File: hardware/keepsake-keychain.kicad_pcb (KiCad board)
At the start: 2 copper layers, 67 parts, among them Q1 MMFTP4042K, Q2 MMFTP4042K, Q3 MMFTP4042K, Q4 MMFTP4042K, SW1 SPDT Power Switch, SW2 PTS636 SK25J SMTR LFS, U1 74HC595 RED Shift Register, U2 74HC595 GREEN Shift Register, U3 74HC595 BLUE Shift Register, U4 Op Amp, U5 ATTINY1614, U6 MEMS Microphone

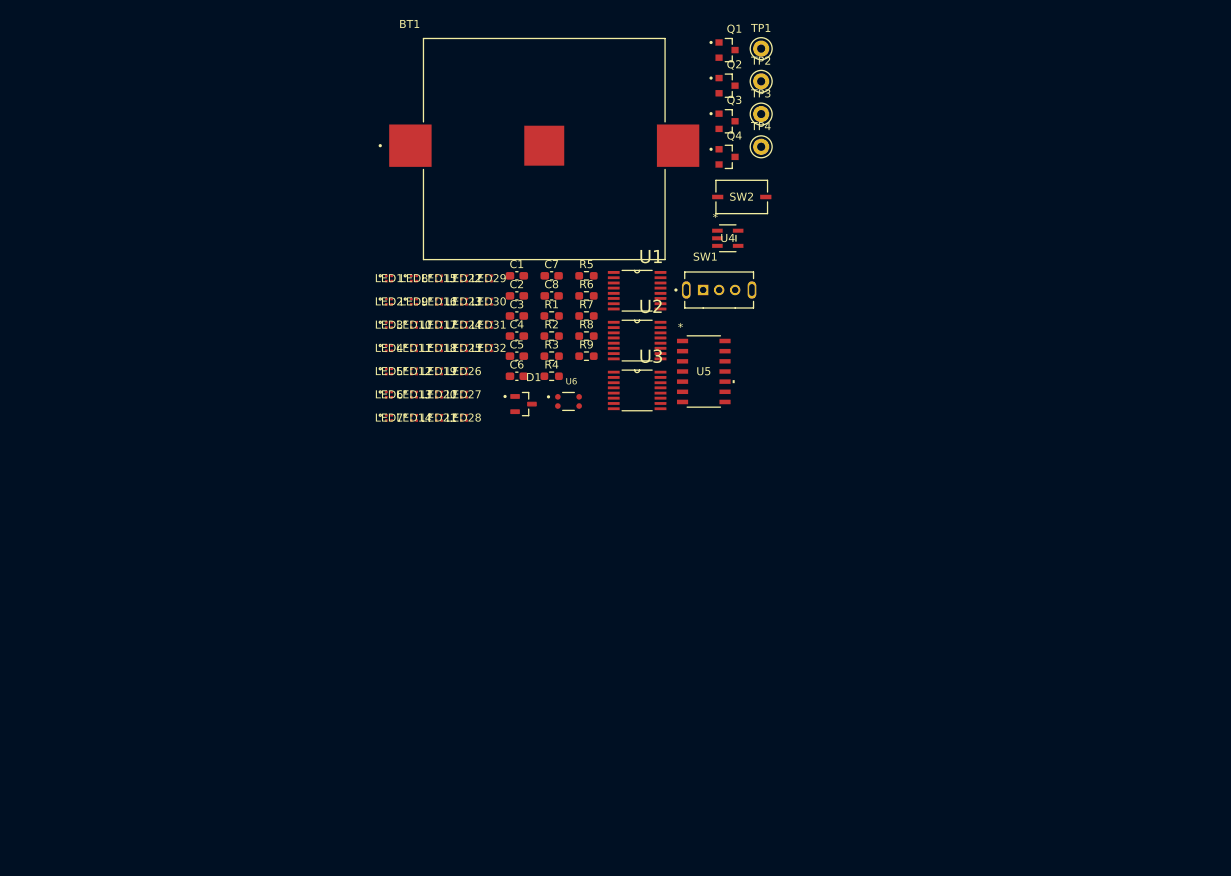
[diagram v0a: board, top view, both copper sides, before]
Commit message: Swap push button and slide switch for better options
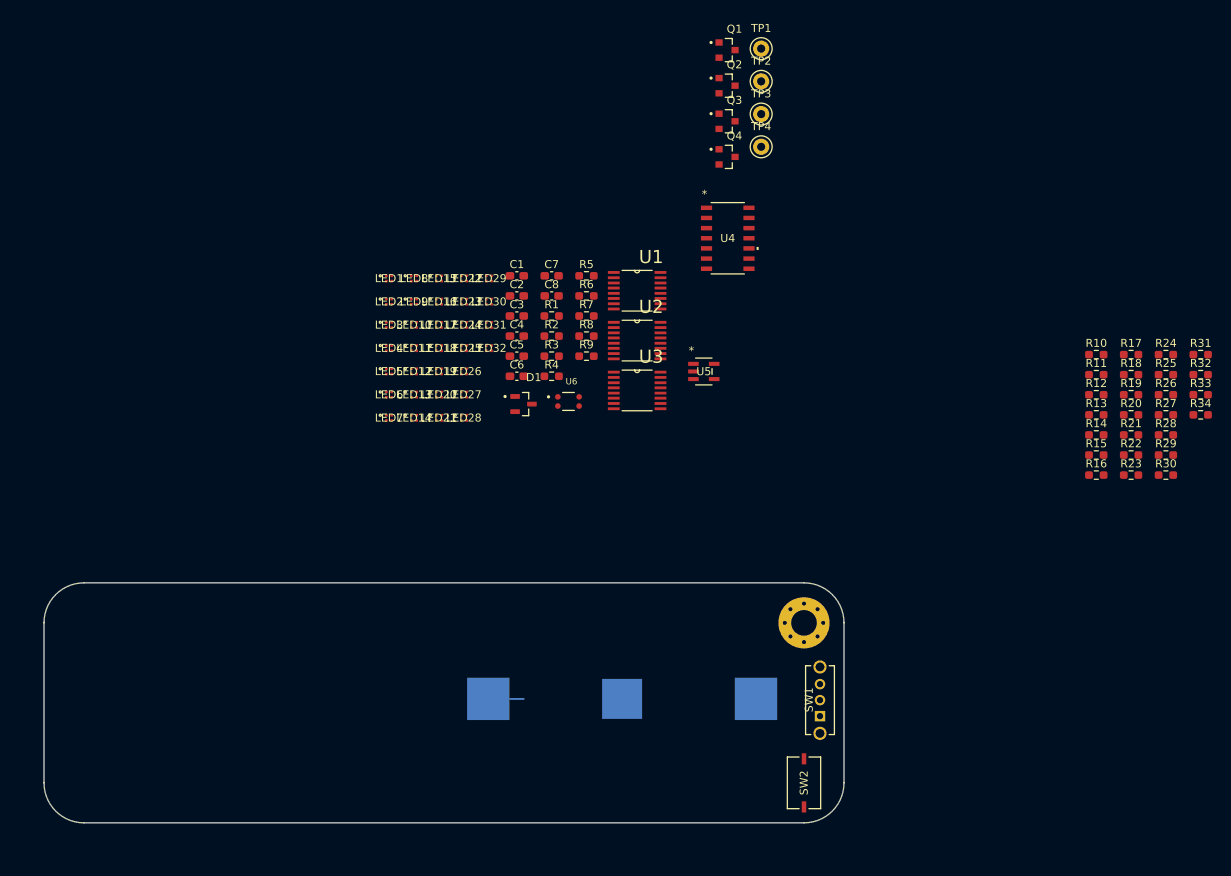
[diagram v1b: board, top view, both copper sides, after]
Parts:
- added H1: MountingHole, MountingHole:MountingHole_3.2mm_M3_Pad_Via, F.Cu at (178.5, 108.0)
- added R10: 100, Resistor_SMD:R_0603_1608Metric_Pad0.98x0.95mm_HandSolder, F.Cu at (215.0, 74.5)
- added R11: 120, Resistor_SMD:R_0603_1608Metric_Pad0.98x0.95mm_HandSolder, F.Cu at (215.0, 77.0)
- added R12: 180, Resistor_SMD:R_0603_1608Metric_Pad0.98x0.95mm_HandSolder, F.Cu at (215.0, 79.5)
- added R13: 100, Resistor_SMD:R_0603_1608Metric_Pad0.98x0.95mm_HandSolder, F.Cu at (215.0, 82.0)
- added R14: 120, Resistor_SMD:R_0603_1608Metric_Pad0.98x0.95mm_HandSolder, F.Cu at (215.0, 84.5)
- added R15: 180, Resistor_SMD:R_0603_1608Metric_Pad0.98x0.95mm_HandSolder, F.Cu at (215.0, 87.0)
- added R16: 100, Resistor_SMD:R_0603_1608Metric_Pad0.98x0.95mm_HandSolder, F.Cu at (215.0, 89.5)
- added R17: 120, Resistor_SMD:R_0603_1608Metric_Pad0.98x0.95mm_HandSolder, F.Cu at (219.4, 74.5)
- added R18: 180, Resistor_SMD:R_0603_1608Metric_Pad0.98x0.95mm_HandSolder, F.Cu at (219.4, 77.0)
- added R19: 100, Resistor_SMD:R_0603_1608Metric_Pad0.98x0.95mm_HandSolder, F.Cu at (219.4, 79.5)
- added R20: 120, Resistor_SMD:R_0603_1608Metric_Pad0.98x0.95mm_HandSolder, F.Cu at (219.4, 82.0)
- added R21: 180, Resistor_SMD:R_0603_1608Metric_Pad0.98x0.95mm_HandSolder, F.Cu at (219.4, 84.5)
- added R22: 100, Resistor_SMD:R_0603_1608Metric_Pad0.98x0.95mm_HandSolder, F.Cu at (219.4, 87.0)
- added R23: 120, Resistor_SMD:R_0603_1608Metric_Pad0.98x0.95mm_HandSolder, F.Cu at (219.4, 89.5)
- added R24: 180, Resistor_SMD:R_0603_1608Metric_Pad0.98x0.95mm_HandSolder, F.Cu at (223.7, 74.5)
- added R25: 390K, Resistor_SMD:R_0603_1608Metric_Pad0.98x0.95mm_HandSolder, F.Cu at (223.7, 77.0)
- added R26: 10K, Resistor_SMD:R_0603_1608Metric_Pad0.98x0.95mm_HandSolder, F.Cu at (223.7, 79.5)
- added R27: 100K, Resistor_SMD:R_0603_1608Metric_Pad0.98x0.95mm_HandSolder, F.Cu at (223.7, 82.0)
- added R28: 10K, Resistor_SMD:R_0603_1608Metric_Pad0.98x0.95mm_HandSolder, F.Cu at (223.7, 84.5)
- added R29: 100K, Resistor_SMD:R_0603_1608Metric_Pad0.98x0.95mm_HandSolder, F.Cu at (223.7, 87.0)
- added R30: 100K, Resistor_SMD:R_0603_1608Metric_Pad0.98x0.95mm_HandSolder, F.Cu at (223.7, 89.5)
- added R31: 100K, Resistor_SMD:R_0603_1608Metric_Pad0.98x0.95mm_HandSolder, F.Cu at (228.1, 74.5)
- added R32: 100K, Resistor_SMD:R_0603_1608Metric_Pad0.98x0.95mm_HandSolder, F.Cu at (228.1, 77.0)
- added R33: 100K, Resistor_SMD:R_0603_1608Metric_Pad0.98x0.95mm_HandSolder, F.Cu at (228.1, 79.5)
- added R34: 100K, Resistor_SMD:R_0603_1608Metric_Pad0.98x0.95mm_HandSolder, F.Cu at (228.1, 82.0)
- BT1: moved to B.Cu
- R1: value 390K -> 100
- R2, R5, R8: value 100K -> 120
- R3: value 10K -> 180
- R4, R7: value 100K -> 100
- R6, R9: value 100K -> 180
- SW2: footprint 0_Push_Button:SW_PTS636_SK25J_SMTR_LFS_CNK -> 0_Tactile_Push_Button:SW_PTS636_SK25J_SMTR_LFS_CNK
- U1: value 74HC595 RED Shift Register -> 74HC595 BLUE Shift Register
- U3: value 74HC595 BLUE Shift Register -> 74HC595 RED Shift Register
- U4: value Op Amp -> ATTINY1614; footprint 0_Op_Amp:SOT-23-5_MC_MCH -> 0_ATtiny1614:SOIC14_SL_MCH
- U5: value ATTINY1614 -> Op Amp; footprint 0_ATtiny1614:SOIC14_SL_MCH -> 0_Op_Amp:SOT-23-5_MC_MCH
- moved SW2 73.6 mm to (178.5, 128.0), turned to 90 degrees
- moved BT1 69.8 mm to (155.8, 117.5), turned to 180 degrees
- moved SW1 52.8 mm to (180.5, 117.7), turned to 90 degrees
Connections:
- C7 pad 2: Net-(U4-VIN+) -> Net-(U5-VIN+)
- D1 pad 1: Net-(U4-VOUT) -> Net-(U5-VOUT)
- LED1 pad 1: unconnected-(LED1-Pad1) -> BLUE_0
- LED1 pad 2: unconnected-(LED1-Pad2) -> GREEN_0
- LED1 pad 3: unconnected-(LED1-Pad3) -> RED_0
- LED10 pad 1: unconnected-(LED10-Pad1) -> BLUE_2
- LED10 pad 2: unconnected-(LED10-Pad2) -> GREEN_2
- LED10 pad 3: unconnected-(LED10-Pad3) -> RED_2
- LED11 pad 1: unconnected-(LED11-Pad1) -> BLUE_4
- LED11 pad 2: unconnected-(LED11-Pad2) -> GREEN_4
- LED11 pad 3: unconnected-(LED11-Pad3) -> RED_4
- LED12 pad 1: unconnected-(LED12-Pad1) -> BLUE_6
- LED12 pad 2: unconnected-(LED12-Pad2) -> GREEN_6
- LED12 pad 3: unconnected-(LED12-Pad3) -> RED_6
- LED13 pad 1: unconnected-(LED13-Pad1) -> BLUE_1
- LED13 pad 2: unconnected-(LED13-Pad2) -> GREEN_1
- LED13 pad 3: unconnected-(LED13-Pad3) -> RED_1
- LED14 pad 1: unconnected-(LED14-Pad1) -> BLUE_3
- LED14 pad 2: unconnected-(LED14-Pad2) -> GREEN_3
- LED14 pad 3: unconnected-(LED14-Pad3) -> RED_3
- LED15 pad 1: unconnected-(LED15-Pad1) -> BLUE_5
- LED15 pad 2: unconnected-(LED15-Pad2) -> GREEN_5
- LED15 pad 3: unconnected-(LED15-Pad3) -> RED_5
- LED16 pad 1: unconnected-(LED16-Pad1) -> BLUE_7
- LED16 pad 2: unconnected-(LED16-Pad2) -> GREEN_7
- LED16 pad 3: unconnected-(LED16-Pad3) -> RED_7
- LED17 pad 1: unconnected-(LED17-Pad1) -> BLUE_0
- LED17 pad 2: unconnected-(LED17-Pad2) -> GREEN_0
- LED17 pad 3: unconnected-(LED17-Pad3) -> RED_0
- LED18 pad 1: unconnected-(LED18-Pad1) -> BLUE_2
- LED18 pad 2: unconnected-(LED18-Pad2) -> GREEN_2
- LED18 pad 3: unconnected-(LED18-Pad3) -> RED_2
- LED19 pad 1: unconnected-(LED19-Pad1) -> BLUE_4
- LED19 pad 2: unconnected-(LED19-Pad2) -> GREEN_4
- LED19 pad 3: unconnected-(LED19-Pad3) -> RED_4
- LED2 pad 1: unconnected-(LED2-Pad1) -> BLUE_2
- LED2 pad 2: unconnected-(LED2-Pad2) -> GREEN_2
- LED2 pad 3: unconnected-(LED2-Pad3) -> RED_2
- LED20 pad 1: unconnected-(LED20-Pad1) -> BLUE_6
- LED20 pad 2: unconnected-(LED20-Pad2) -> GREEN_6
- LED20 pad 3: unconnected-(LED20-Pad3) -> RED_6
- LED21 pad 1: unconnected-(LED21-Pad1) -> BLUE_1
- LED21 pad 2: unconnected-(LED21-Pad2) -> GREEN_1
- LED21 pad 3: unconnected-(LED21-Pad3) -> RED_1
- LED22 pad 1: unconnected-(LED22-Pad1) -> BLUE_3
- LED22 pad 2: unconnected-(LED22-Pad2) -> GREEN_3
- LED22 pad 3: unconnected-(LED22-Pad3) -> RED_3
- LED23 pad 1: unconnected-(LED23-Pad1) -> BLUE_5
- LED23 pad 2: unconnected-(LED23-Pad2) -> GREEN_5
- LED23 pad 3: unconnected-(LED23-Pad3) -> RED_5
- LED24 pad 1: unconnected-(LED24-Pad1) -> BLUE_7
- LED24 pad 2: unconnected-(LED24-Pad2) -> GREEN_7
- LED24 pad 3: unconnected-(LED24-Pad3) -> RED_7
- LED25 pad 1: unconnected-(LED25-Pad1) -> BLUE_0
- LED25 pad 2: unconnected-(LED25-Pad2) -> GREEN_0
- LED25 pad 3: unconnected-(LED25-Pad3) -> RED_0
- LED26 pad 1: unconnected-(LED26-Pad1) -> BLUE_2
- LED26 pad 2: unconnected-(LED26-Pad2) -> GREEN_2
- LED26 pad 3: unconnected-(LED26-Pad3) -> RED_2
- LED27 pad 1: unconnected-(LED27-Pad1) -> BLUE_4
- LED27 pad 2: unconnected-(LED27-Pad2) -> GREEN_4
- LED27 pad 3: unconnected-(LED27-Pad3) -> RED_4
- LED28 pad 1: unconnected-(LED28-Pad1) -> BLUE_6
- LED28 pad 2: unconnected-(LED28-Pad2) -> GREEN_6
- LED28 pad 3: unconnected-(LED28-Pad3) -> RED_6
- LED29 pad 1: unconnected-(LED29-Pad1) -> BLUE_1
- LED29 pad 2: unconnected-(LED29-Pad2) -> GREEN_1
- LED29 pad 3: unconnected-(LED29-Pad3) -> RED_1
- LED3 pad 1: unconnected-(LED3-Pad1) -> BLUE_4
- LED3 pad 2: unconnected-(LED3-Pad2) -> GREEN_4
- LED3 pad 3: unconnected-(LED3-Pad3) -> RED_4
- LED30 pad 1: unconnected-(LED30-Pad1) -> BLUE_3
- LED30 pad 2: unconnected-(LED30-Pad2) -> GREEN_3
- LED30 pad 3: unconnected-(LED30-Pad3) -> RED_3
- LED31 pad 1: unconnected-(LED31-Pad1) -> BLUE_5
- LED31 pad 2: unconnected-(LED31-Pad2) -> GREEN_5
- LED31 pad 3: unconnected-(LED31-Pad3) -> RED_5
- LED32 pad 1: unconnected-(LED32-Pad1) -> BLUE_7
- LED32 pad 2: unconnected-(LED32-Pad2) -> GREEN_7
- LED32 pad 3: unconnected-(LED32-Pad3) -> RED_7
- LED4 pad 1: unconnected-(LED4-Pad1) -> BLUE_6
- LED4 pad 2: unconnected-(LED4-Pad2) -> GREEN_6
- LED4 pad 3: unconnected-(LED4-Pad3) -> RED_6
- LED5 pad 1: unconnected-(LED5-Pad1) -> BLUE_1
- LED5 pad 2: unconnected-(LED5-Pad2) -> GREEN_1
- LED5 pad 3: unconnected-(LED5-Pad3) -> RED_1
- LED6 pad 1: unconnected-(LED6-Pad1) -> BLUE_3
- LED6 pad 2: unconnected-(LED6-Pad2) -> GREEN_3
- LED6 pad 3: unconnected-(LED6-Pad3) -> RED_3
- LED7 pad 1: unconnected-(LED7-Pad1) -> BLUE_5
- LED7 pad 2: unconnected-(LED7-Pad2) -> GREEN_5
- LED7 pad 3: unconnected-(LED7-Pad3) -> RED_5
- LED8 pad 1: unconnected-(LED8-Pad1) -> BLUE_7
- LED8 pad 2: unconnected-(LED8-Pad2) -> GREEN_7
- LED8 pad 3: unconnected-(LED8-Pad3) -> RED_7
- LED9 pad 1: unconnected-(LED9-Pad1) -> BLUE_0
- LED9 pad 2: unconnected-(LED9-Pad2) -> GREEN_0
- LED9 pad 3: unconnected-(LED9-Pad3) -> RED_0
- Q1 pad 1: Net-(Q1-Pad1) -> S_ROW_0
- Q2 pad 1: Net-(Q2-Pad1) -> S_ROW_1
- Q3 pad 1: Net-(Q3-Pad1) -> S_ROW_2
- Q4 pad 1: Net-(Q4-Pad1) -> S_ROW_3
- R1 pad 1: Net-(U4-VOUT) -> BLUE_0
- R1 pad 2: Net-(U4-VIN-) -> Net-(U1-Q0)
- R2 pad 1: +3V3 -> GREEN_0
- R2 pad 2: /BIAS -> Net-(U2-Q0)
- R3 pad 1: Net-(U4-VIN-) -> RED_0
- R3 pad 2: /BIAS -> Net-(U3-Q0)
- R4 pad 1: /BIAS -> BLUE_1
- R4 pad 2: GND -> Net-(U1-Q1)
- R5 pad 1: MIC -> GREEN_1
- R5 pad 2: GND -> Net-(U2-Q1)
- R6 pad 1: S_ROW_0 -> RED_1
- R6 pad 2: Net-(Q1-Pad1) -> Net-(U3-Q1)
- R7 pad 1: S_ROW_1 -> BLUE_2
- R7 pad 2: Net-(Q2-Pad1) -> Net-(U1-Q2)
- R8 pad 1: S_ROW_2 -> GREEN_2
- R8 pad 2: Net-(Q3-Pad1) -> Net-(U2-Q2)
- R9 pad 1: S_ROW_3 -> RED_2
- R9 pad 2: Net-(Q4-Pad1) -> Net-(U3-Q2)
- SW2 pad 1: Net-(U5-PB0) -> Net-(U4-PB0)
- TP1 pad 1: MIC -> Net-(U4-PA0/*RESET/UPDI)
- TP2 pad 1: Net-(U5-PA0/*RESET/UPDI) -> MIC
- TP3 pad 1: Net-(U5-TOSC1/PB3) -> Net-(U4-TOSC1/PB3)
- TP4 pad 1: Net-(U5-TOSC2/PB2) -> Net-(U4-TOSC2/PB2)
- U1 pad 1: unconnected-(U1-Q1-Pad1) -> Net-(U1-Q1)
- U1 pad 14: DATA -> Net-(U1-DS)
- U1 pad 15: unconnected-(U1-Q0-Pad15) -> Net-(U1-Q0)
- U1 pad 2: unconnected-(U1-Q2-Pad2) -> Net-(U1-Q2)
- U1 pad 3: unconnected-(U1-Q3-Pad3) -> Net-(U1-Q3)
- U1 pad 4: unconnected-(U1-Q4-Pad4) -> Net-(U1-Q4)
- U1 pad 5: unconnected-(U1-Q5-Pad5) -> Net-(U1-Q5)
- U1 pad 6: unconnected-(U1-Q6-Pad6) -> Net-(U1-Q6)
- U1 pad 7: unconnected-(U1-Q7-Pad7) -> Net-(U1-Q7)
- U2 pad 1: unconnected-(U2-Q1-Pad1) -> Net-(U2-Q1)
- U2 pad 15: unconnected-(U2-Q0-Pad15) -> Net-(U2-Q0)
- U2 pad 2: unconnected-(U2-Q2-Pad2) -> Net-(U2-Q2)
- U2 pad 3: unconnected-(U2-Q3-Pad3) -> Net-(U2-Q3)
- U2 pad 4: unconnected-(U2-Q4-Pad4) -> Net-(U2-Q4)
- U2 pad 5: unconnected-(U2-Q5-Pad5) -> Net-(U2-Q5)
- U2 pad 6: unconnected-(U2-Q6-Pad6) -> Net-(U2-Q6)
- U2 pad 7: unconnected-(U2-Q7-Pad7) -> Net-(U2-Q7)
- U3 pad 1: unconnected-(U3-Q1-Pad1) -> Net-(U3-Q1)
- U3 pad 15: unconnected-(U3-Q0-Pad15) -> Net-(U3-Q0)
- U3 pad 2: unconnected-(U3-Q2-Pad2) -> Net-(U3-Q2)
- U3 pad 3: unconnected-(U3-Q3-Pad3) -> Net-(U3-Q3)
- U3 pad 4: unconnected-(U3-Q4-Pad4) -> Net-(U3-Q4)
- U3 pad 5: unconnected-(U3-Q5-Pad5) -> Net-(U3-Q5)
- U3 pad 6: unconnected-(U3-Q6-Pad6) -> Net-(U3-Q6)
- U3 pad 7: unconnected-(U3-Q7-Pad7) -> Net-(U3-Q7)
- U4 pad 1: Net-(U4-VOUT) -> +3V3
- U4 pad 2: GND -> S_ROW_0
- U4 pad 3: Net-(U4-VIN+) -> S_ROW_1
- U4 pad 4: Net-(U4-VIN-) -> S_ROW_2
- U4 pad 5: +3V3 -> S_ROW_3
- U5 pad 1: +3V3 -> Net-(U5-VOUT)
- U5 pad 2: S_ROW_0 -> GND
- U5 pad 3: S_ROW_1 -> Net-(U5-VIN+)
- U5 pad 4: S_ROW_2 -> Net-(U5-VIN-)
- U5 pad 5: S_ROW_3 -> +3V3
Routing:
- net Net-(BT1-Pad1): track 0.00 -> 1.73 mm
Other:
- board outline added: 100 x 30 mm

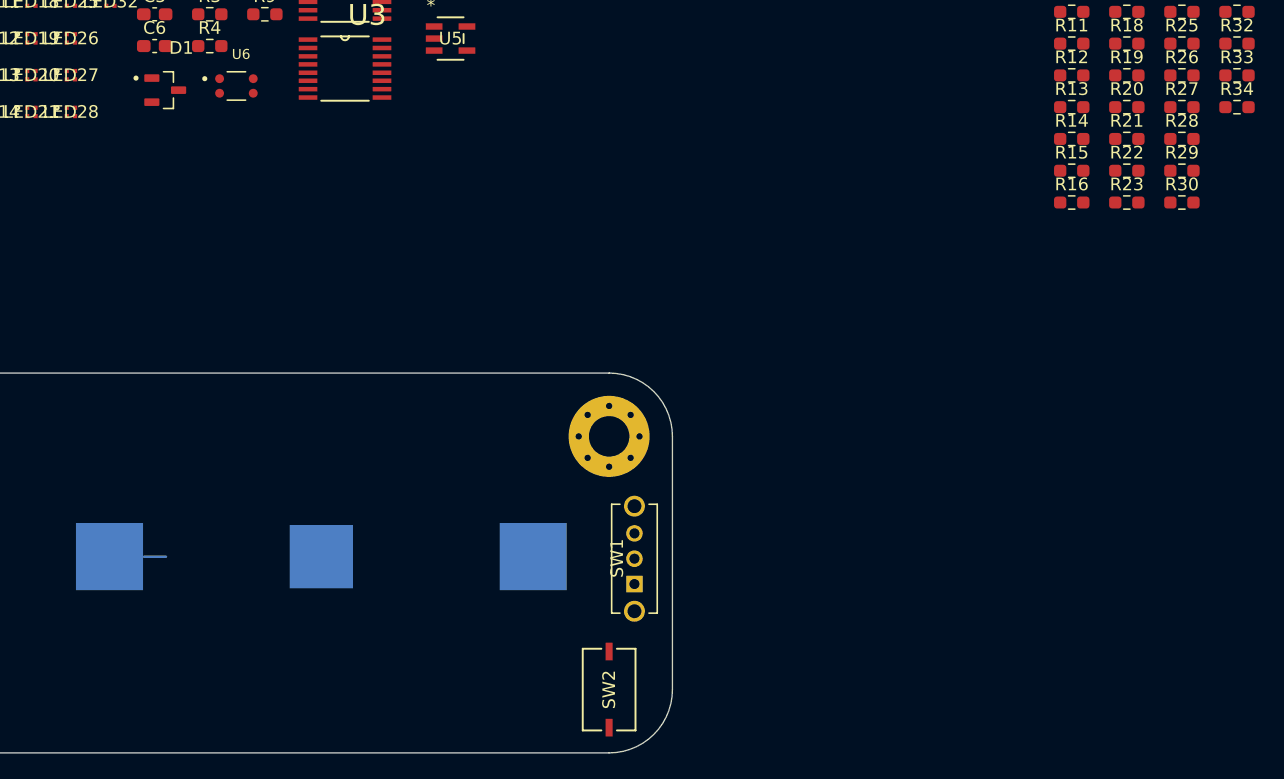
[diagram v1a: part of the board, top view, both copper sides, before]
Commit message: Attach models. Complete schematic, pass ERC.
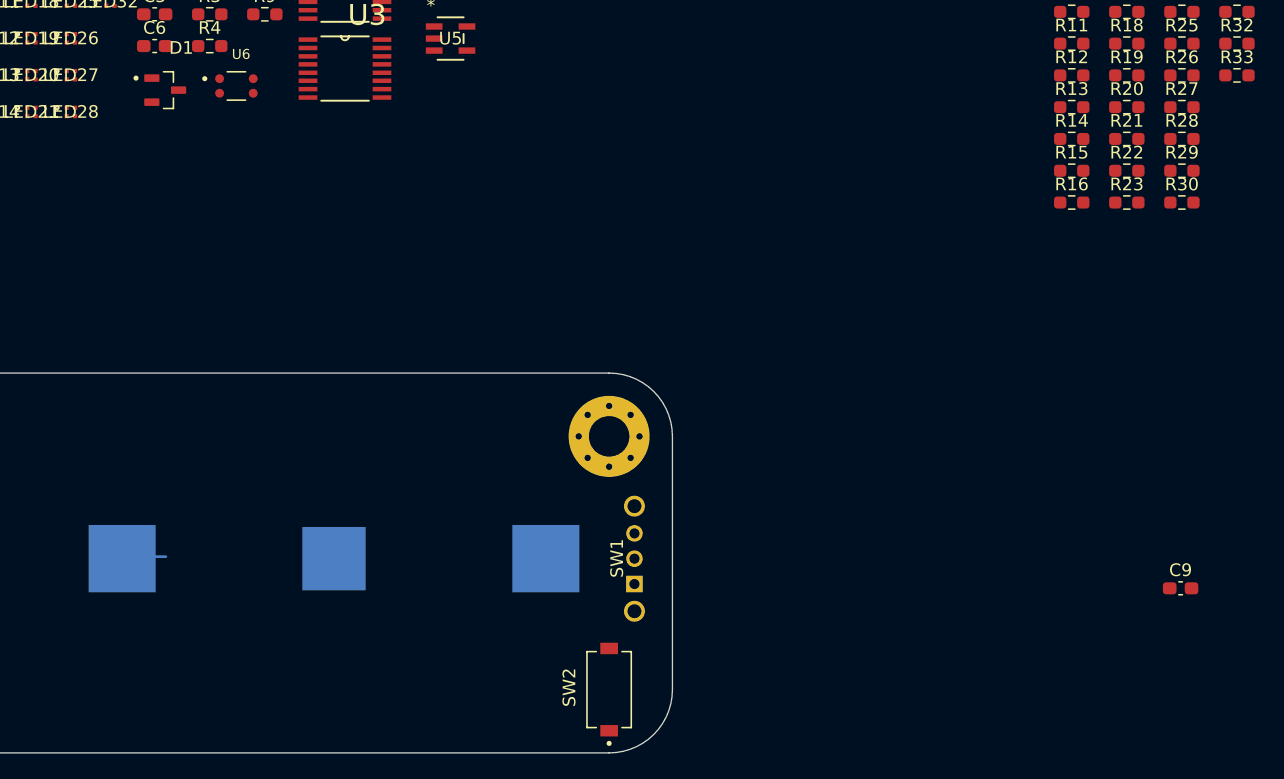
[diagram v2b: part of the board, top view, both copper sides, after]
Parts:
- removed R34: 100K, Resistor_SMD:R_0603_1608Metric_Pad0.98x0.95mm_HandSolder
- added C9: 1uF, Capacitor_SMD:C_0603_1608Metric_Pad1.08x0.95mm_HandSolder, F.Cu at (223.6, 120.0)
- R25: value 390K -> 220K
- SW2: footprint 0_Tactile_Push_Button:SW_PTS636_SK25J_SMTR_LFS_CNK -> 0_Tactile_Push_Button:SW_PTS636_SM43J_SMTR_LFS
- moved BT1 1.01 mm to (156.8, 117.7)
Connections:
- BT1 pad 1_1: Net-(BT1-Pad1) -> (no net)
- C1 pad 1: GND -> +3V3
- C1 pad 2: +3V3 -> GND
- C2 pad 1: GND -> +3V3
- C2 pad 2: +3V3 -> GND
- C3 pad 1: GND -> +3V3
- C3 pad 2: +3V3 -> GND
- C6 pad 1: GND -> +3V3
- C6 pad 2: MIC -> GND
- C7 pad 1: Net-(U6-OUTPUT) -> GND
- C7 pad 2: Net-(U5-VIN+) -> MIC
- C8 pad 1: /BIAS -> Net-(U6-OUTPUT)
- C8 pad 2: GND -> Net-(U5-VIN+)
- R29 pad 1: MIC -> /BIAS
- R30 pad 1: /BIAS -> S_ROW_0
- R30 pad 2: GND -> +3V3
- R31 pad 1: S_ROW_0 -> S_ROW_1
- R32 pad 1: S_ROW_1 -> S_ROW_2
- R33 pad 1: S_ROW_2 -> S_ROW_3

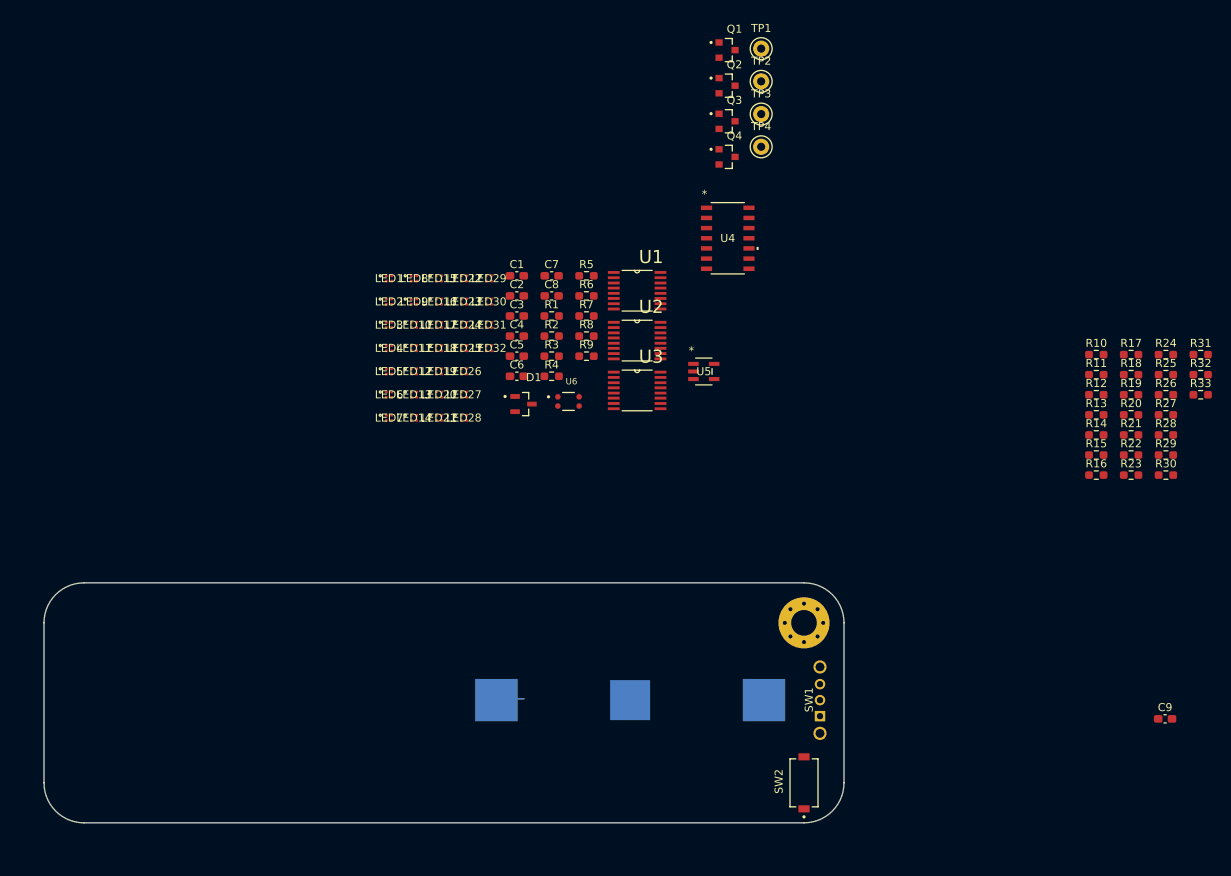
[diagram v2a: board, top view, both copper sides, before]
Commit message: Place LED passives in line
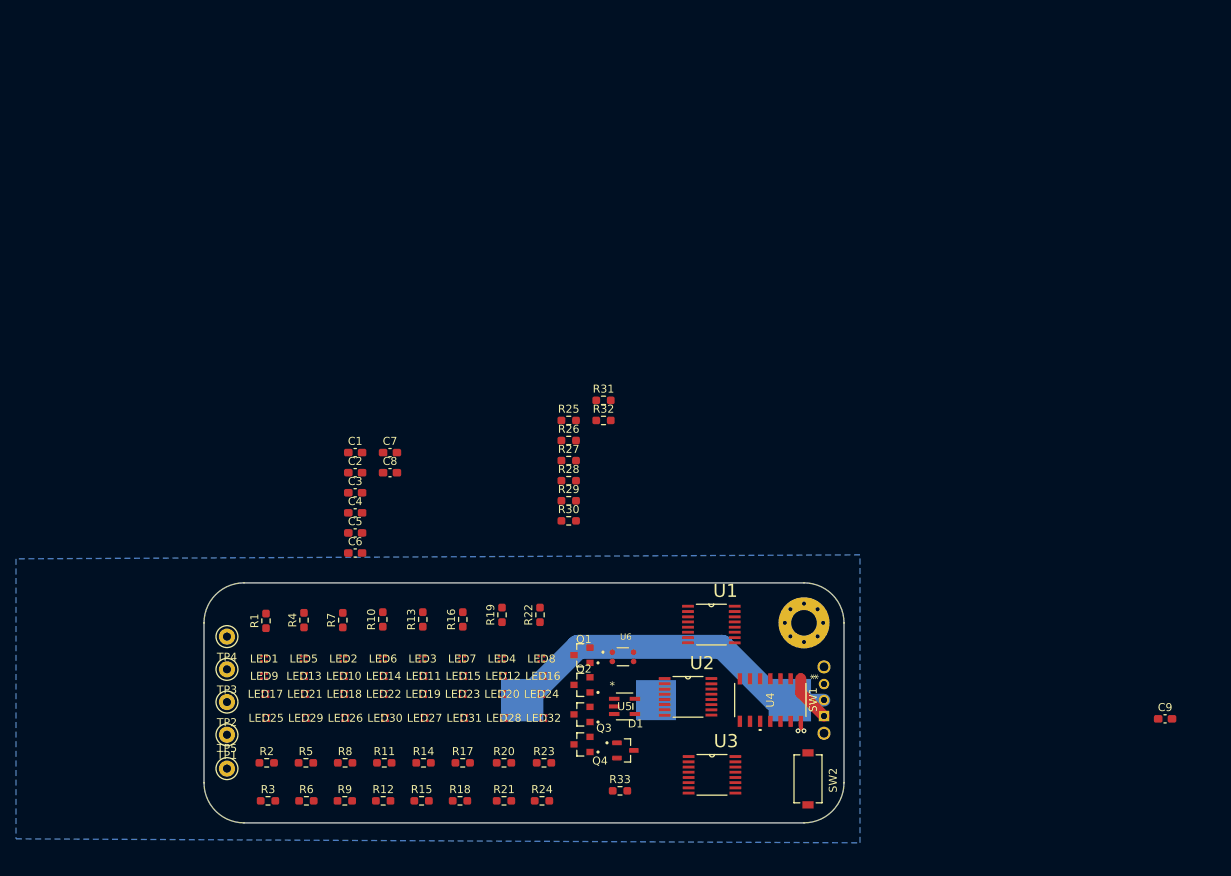
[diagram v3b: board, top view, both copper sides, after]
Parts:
- added TP5: 5002, digikey-footprints:Test_Point_D1.02mm, F.Cu at (106.4, 126.2)
- moved TP1 108.7 mm to (106.4, 122.0), turned to 180 degrees
- moved R12 102.6 mm to (125.9, 130.2)
- moved TP2 102.4 mm to (106.4, 117.9), turned to 180 degrees
- moved R11 101.4 mm to (126.0, 125.5)
- moved R18 99.4 mm to (135.5, 130.2)
- moved R17 97.9 mm to (135.8, 125.5)
- moved TP3 96.3 mm to (106.4, 113.8), turned to 180 degrees
- moved R24 95.9 mm to (145.8, 130.2)
- moved R10 95.1 mm to (125.8, 107.6), turned to 90 degrees
- moved R15 94.8 mm to (130.7, 130.2)
- moved R14 93.6 mm to (130.9, 125.5)
- moved R21 90.8 mm to (141.0, 130.2)
- moved TP4 90.6 mm to (106.4, 109.7), turned to 180 degrees
- moved R20 89.6 mm to (141.0, 125.5)
- moved R13 88.0 mm to (130.8, 107.6), turned to 90 degrees
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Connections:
- TP1 pad 1: Net-(U4-PA0/*RESET/UPDI) -> GND
- TP2 pad 1: MIC -> Net-(U4-PA0/*RESET/UPDI)
- TP3 pad 1: Net-(U4-TOSC1/PB3) -> MIC
- TP4 pad 1: Net-(U4-TOSC2/PB2) -> Net-(U4-TOSC1/PB3)
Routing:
- net Net-(BT1-Pad1): track 1.73 -> 43.3 mm
- net +3V3: track 0.00 -> 5.85 mm
- net GND: track 0.00 -> 2.69 mm, vias 0 -> 2
- added copper zone on B.Cu, net GND
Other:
- board size 100 x 30 mm -> 80 x 30 mm
